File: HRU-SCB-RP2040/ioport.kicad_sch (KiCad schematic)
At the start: 3 parts, among them J28 Conn_01x04_Socket

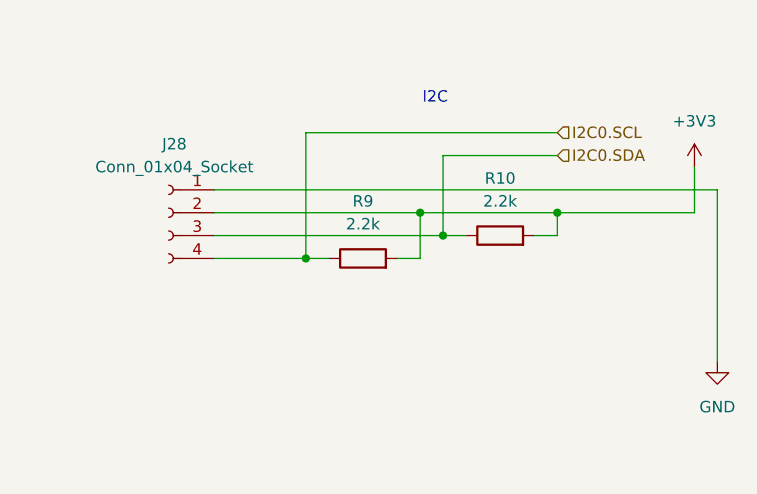
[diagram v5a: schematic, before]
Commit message: Update: apply super DCDC
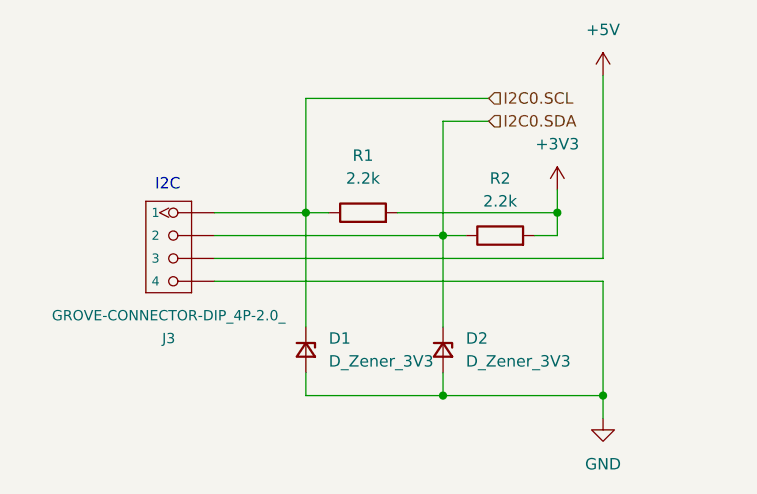
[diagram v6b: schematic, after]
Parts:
- removed J28: Conn_01x04_Socket, Connector_PinHeader_2.00mm:PinHeader_1x04_P2.00mm_Vertical, symbol Connector:Conn_01x04_Socket
- added D1, D2: D_Zener_3V3, Diode_THT:D_T-1_P5.08mm_Horizontal, symbol Device:D_Zener_Small
- added J3: GROVE-CONNECTOR-DIP_4P-2.0_, OPL_Connector:GROVE-HW4-2.0, symbol OPL_Connector:GROVE-CONNECTOR-DIP_4P-2.0_
- renumbered R9 to R1, R10 to R2
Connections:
- net GND: now also D1.2 (A), D2.2 (A), J3.4
- net I2C0.SCL: now also D1.1 (K), J3.1
- net I2C0.SDA: now also D2.1 (K), J3.2
- new net +5V: J3.3
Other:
- moved on the sheet: R1

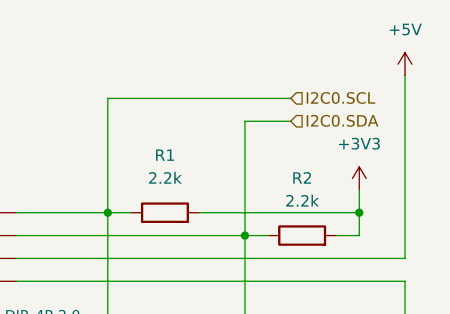
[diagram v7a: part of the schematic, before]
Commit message: fix(HRU-SCB-RP2040): assign 3V3 to I2C's VCC and refactor parts layout
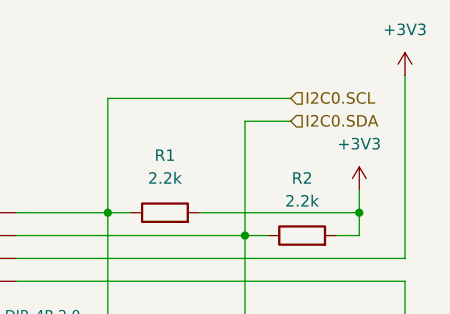
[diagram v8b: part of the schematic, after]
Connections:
- net +5V is gone; now on net +3V3: J3.3
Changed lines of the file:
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@@
-	)
-	(symbol
-		(lib_id "power:+5V")
-		(at 88.9 76.2 0)
-		(unit 1)
-		(body_style 1)
-		(exclude_from_sim no)
-		(in_bom yes)
-		(on_board yes)
-		(in_pos_files yes)
-		(dnp no)
-		(fields_autoplaced yes)
-		(property "Reference" "#PWR06"
-			(at 88.9 80.01 0)
-			(hide yes)
-			(show_name no)
-			(do_not_autoplace no)
-			(effects
-				(font
-					(size 1.27 1.27)
-				)
-			)
-		)
-		(property "Value" "+5V"
-			(at 88.9 71.12 0)
-			(show_name no)
-			(do_not_autoplace no)
-			(effects
-				(font
-					(size 1.27 1.27)
-				)
-			)
-		)
-		(property "Footprint" ""
-			(at 88.9 76.2 0)
-			(hide yes)
-			(show_name no)
-			(do_not_autoplace no)
-			(effects
-				(font
-					(size 1.27 1.27)
-				)
-			)
-		)
-		(property "Datasheet" ""
-			(at 88.9 76.2 0)
-			(hide yes)
-			(show_name no)
-			(do_not_autoplace no)
-			(effects
-				(font
-					(size 1.27 1.27)
-				)
-			)
-		)
-		(property "Description" "Power symbol creates a global label with name \"+5V\""
-			(at 88.9 76.2 0)
-			(hide yes)
-			(show_name no)
-			(do_not_autoplace no)
-			(effects
-				(font
-					(size 1.27 1.27)
-				)
-			)
-		)
-		(pin "1"
-		)
-		(instances
-			(project "HRU-SCB-RP2040"
-				(path "/22d57d1f-fa00-4148-a62a-8eb596ebbd21/e77e8245-6b3f-4da7-90e6-d027ac806a87"
-					(reference "#PWR06")
-					(unit 1)
-				)
-			)
-		)
 	)
 	(symbol
@@
 					(unit 1)
 				)
+			)
+		)
+	)
+	(symbol
+		(lib_id "power:+3V3")
+		(at 88.9 76.2 0)
+		(unit 1)
+		(body_style 1)
+		(exclude_from_sim no)
+		(in_bom yes)
+		(on_board yes)
+		(in_pos_files yes)
+		(dnp no)
+		(fields_autoplaced yes)
+		(property "Reference" "#PWR021"
+			(at 88.9 80.01 0)
+			(hide yes)
+			(show_name no)
+			(do_not_autoplace no)
+			(effects
+				(font
+					(size 1.27 1.27)
+				)
+			)
+		)
+		(property "Value" "+3V3"
+			(at 88.9 71.12 0)
+			(show_name no)
+			(do_not_autoplace no)
+			(effects
+				(font
+					(size 1.27 1.27)
+				)
+			)
+		)
+		(property "Footprint" ""
+			(at 88.9 76.2 0)
+			(hide yes)
+			(show_name no)
+			(do_not_autoplace no)
+			(effects
+				(font
+					(size 1.27 1.27)
+				)
+			)
+		)
+		(property "Datasheet" ""
+			(at 88.9 76.2 0)
+			(hide yes)
+			(show_name no)
+			(do_not_autoplace no)
+			(effects
+				(font
+					(size 1.27 1.27)
+				)
+			)
+		)
+		(property "Description" "Power symbol creates a global label with name \"+3V3\""
+			(at 88.9 76.2 0)
+			(hide yes)
+			(show_name no)
+			(do_not_autoplace no)
+			(effects
+				(font
+					(size 1.27 1.27)
+				)
+			)
+		)
+		(pin "1"
+		)
+		(instances
+			(project "HRU-SCB-RP2040"
+				(path "/22d57d1f-fa00-4148-a62a-8eb596ebbd21/e77e8245-6b3f-4da7-90e6-d027ac806a87"
+					(reference "#PWR021")
+					(unit 1)
+				)
